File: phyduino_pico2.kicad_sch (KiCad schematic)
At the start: 7 parts, among them J2 PM2.54-1*8, J3 PM2.54-1*10, J4 PM2.54-1*6, J5 PM2.54-1*8, J7 HC-FPC-0.5-22P-CSH20

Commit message: nigthly commit
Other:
- company: (none) -> University of Toronto, Dept. of Physics
- title: (none) -> Phyduino Pico 2
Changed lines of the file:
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@@
 	(generator_version "10.0")
 	(paper "B")
+	(title_block
+		(title "Phyduino Pico 2")
+		(date "2026-05-04")
+		(rev "A")
+		(company "University of Toronto, Dept. of Physics")
+	)
 	(text "GND"
 		(exclude_from_sim no)

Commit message: Made schematic changes : merged usb_pd sheet with wifi sheet. made system regulators adjustable.
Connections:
- net Microcontroller/D18 renamed Microcontroller/D14
- net Microcontroller/D19 renamed Microcontroller/D15
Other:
- sheet Wifi Interface renamed Communication & Power Delivery
- removed sheet USB Power Delivery
- sheet Communication & Power Delivery ports: added I2C1_SCL, I2C1_SDA, PSW_STATUS, USBPD_FLIP, USBPD_GPIO, USBPD_INT, USB_D_N, USB_D_P, WIFI_AT_UART_CTS, WIFI_AT_UART_RTS, WIFI_AT_UART_RX, WIFI_AT_UART_TX, WIFI_DL_UART_RX, WIFI_DL_UART_TX; removed WIFI_UART_CTS, WIFI_UART_RTS, WIFI_UART_RX, WIFI_UART_SEL, WIFI_UART_TX
- sheet Microcontroller ports: added D14, D15, WIFI_DL_UART_RX, WIFI_DL_UART_TX; removed D18, D19, WIFI_UART_SEL
- note added: "D14/SDA"
- note added: "D15/SCL"
- note removed: "D18/SDA"
- note removed: "D19/SCL"
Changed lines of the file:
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@@
 		)
 	)
-	(text "D19/SCL"
+	(text "D15/SCL"
 		(exclude_from_sim no)
 		(at 240.03 101.6 0)
@@
 		)
 	)
-	(text "D18/SDA"
+	(text "D14/SDA"
 		(exclude_from_sim no)
 		(at 240.03 99.06 0)
@@
 	(text "D12/MISO"
 		(exclude_from_sim no)
-		(at 239.522 88.392 0)
+		(at 240.03 88.392 0)
 		(effects
 			(font
@@
 	(text "~D11/MOSI"
 		(exclude_from_sim no)
-		(at 239.268 86.106 0)
+		(at 240.284 86.106 0)
 		(effects
 			(font
@@
 	(wire
 		(pts
-			(xy 71.12 186.69) (xy 107.95 186.69)
-		)
-		(stroke
-			(width 0)
-			(type default)
-		)
-	)
-	(wire
-		(pts
 			(xy 231.14 165.1) (xy 232.41 165.1)
 		)
@@
 	(wire
 		(pts
+			(xy 71.12 165.1) (xy 88.9 165.1)
+		)
+		(stroke
+			(width 0)
+			(type default)
+		)
+	)
+	(wire
+		(pts
 			(xy 232.41 57.15) (xy 143.51 57.15)
 		)
@@
 	(wire
 		(pts
-			(xy 71.12 137.16) (xy 107.95 137.16)
+			(xy 71.12 144.78) (xy 107.95 144.78)
 		)
 		(stroke
@@
 	(wire
 		(pts
+			(xy 71.12 167.64) (xy 88.9 167.64)
+		)
+		(stroke
+			(width 0)
+			(type default)
+		)
+	)
+	(wire
+		(pts
+			(xy 91.44 165.1) (xy 107.95 165.1)
+		)
+		(stroke
+			(width 0)
+			(type default)
+		)
+	)
+	(wire
+		(pts
 			(xy 232.41 54.61) (xy 143.51 54.61)
 		)
@@
 	(wire
 		(pts
+			(xy 88.9 167.64) (xy 91.44 165.1)
+		)
+		(stroke
+			(width 0)
+			(type default)
+		)
+	)
+	(wire
+		(pts
 			(xy 71.12 124.46) (xy 107.95 124.46)
 		)
@@
 	(wire
 		(pts
+			(xy 71.12 147.32) (xy 107.95 147.32)
+		)
+		(stroke
+			(width 0)
+			(type default)
+		)
+	)
+	(wire
+		(pts
 			(xy 48.26 69.85) (xy 48.26 74.93)
 		)
@@
 	(wire
 		(pts
+			(xy 91.44 167.64) (xy 107.95 167.64)
+		)
+		(stroke
+			(width 0)
+			(type default)
+		)
+	)
+	(wire
+		(pts
 			(xy 231.14 127) (xy 232.41 127)
 		)
@@
 	(wire
 		(pts
-			(xy 71.12 139.7) (xy 107.95 139.7)
+			(xy 143.51 114.3) (xy 232.41 114.3)
 		)
 		(stroke
@@
 	(wire
 		(pts
-			(xy 143.51 114.3) (xy 232.41 114.3)
+			(xy 232.41 72.39) (xy 143.51 72.39)
 		)
 		(stroke
@@
 	(wire
 		(pts
-			(xy 232.41 72.39) (xy 143.51 72.39)
+			(xy 58.42 64.77) (xy 45.72 64.77)
 		)
 		(stroke
@@
 	(wire
 		(pts
-			(xy 58.42 64.77) (xy 45.72 64.77)
+			(xy 88.9 165.1) (xy 91.44 167.64)
 		)
 		(stroke
@@
 			)
 		)
-		(pin "D18" bidirectional
+		(pin "D14" bidirectional
 			(at 143.51 97.79 0)
 			(effects
@@
 			)
 		)
-		(pin "D19" bidirectional
+		(pin "D15" bidirectional
 			(at 143.51 100.33 0)
 			(effects
@@
 		)
 		(pin "USB_D_N" bidirectional
-			(at 107.95 139.7 180)
+			(at 107.95 147.32 180)
 			(effects
 				(font
@@
 		)
 		(pin "USB_D_P" bidirectional
-			(at 107.95 137.16 180)
+			(at 107.95 144.78 180)
 			(effects
 				(font
@@
 			)
 		)
-		(pin "WIFI_UART_SEL" output
-			(at 107.95 186.69 180)
+		(pin "WIFI_DL_UART_RX" input
+			(at 107.95 167.64 180)
+			(effects
+				(font
+					(size 1.27 1.27)
+				)
+				(justify left)
+			)
+		)
+		(pin "WIFI_DL_UART_TX" output
+			(at 107.95 165.1 180)
 			(effects
 				(font
@@
 	(sheet
 		(at 39.37 111.76)
-		(size 31.75 30.48)
+		(size 31.75 80.01)
 		(exclude_from_sim no)
 		(in_bom yes)
@@
 			(color 255 255 194 1)
 		)
-		(property "Sheetname" "USB Power Delivery"
+		(property "Sheetname" "Communication & Power Delivery"
 			(at 39.37 111.0484 0)
 			(show_name no)
@@
 			)
 		)
-		(property "Sheetfile" "phyduino_pico2_usbpd.kicad_sch"
-			(at 39.37 142.8246 0)
+		(property "Sheetfile" "phyduino_pico2_wifi.kicad_sch"
+			(at 39.37 192.3546 0)
 			(hide yes)
 			(show_name no)
@@
 			)
 		)
-		(pin "I2C1_SCL" input
-			(at 71.12 116.84 0)
+		(pin "WIFI_ENA" input
+			(at 71.12 189.23 0)
 			(effects
 				(font
@@
 			)
 		)
-		(pin "I2C1_SDA" bidirectional
-			(at 71.12 114.3 0)
+		(pin "WIFI_AT_UART_CTS" output
+			(at 71.12 179.07 0)
 			(effects
 				(font
@@
 			)
 		)
-		(pin "USBPD_FLIP" output
-			(at 71.12 124.46 0)
+		(pin "WIFI_AT_UART_RTS" input
+			(at 71.12 181.61 0)
 			(effects
 				(font
@@
 			)
 		)
-		(pin "USBPD_GPIO" output
-			(at 71.12 127 0)
+		(pin "WIFI_AT_UART_RX" input
+			(at 71.12 176.53 0)
 			(effects
 				(font
@@
 			)
 		)
-		(pin "USBPD_INT" output
-			(at 71.12 121.92 0)
+		(pin "WIFI_AT_UART_TX" output
+			(at 71.12 173.99 0)
 			(effects
 				(font
@@
 			)
 		)
-		(pin "PSW_STATUS" output
-			(at 71.12 130.81 0)
+		(pin "WIFI_DL_UART_RX" input
+			(at 71.12 167.64 0)
 			(effects
 				(font
@@
 			)
 		)
-		(pin "USB_D_N" bidirectional
-			(at 71.12 139.7 0)
+		(pin "WIFI_DL_UART_TX" output
+			(at 71.12 165.1 0)
 			(effects
 				(font
@@
 			)
 		)
-		(pin "USB_D_P" bidirectional
-			(at 71.12 137.16 0)
+		(pin "I2C1_SCL" input
+			(at 71.12 116.84 0)
 			(effects
 				(font
@@
 			)
 		)
-		(instances
-			(project "phyduino_pico2"
-				(path "/42309c5d-9d7a-429d-b353-e8927a604374"
-					(page "4")
-				)
-			)
-		)
-	)
-	(sheet
-		(at 39.37 171.45)
-		(size 31.75 20.32)
-		(exclude_from_sim no)
-		(in_bom yes)
-		(on_board yes)
-		(dnp no)
-		(fields_autoplaced yes)
-		(stroke
-			(width 0.1524)
-			(type solid)
-		)
-		(fill
-			(color 255 255 194 1)
-		)
-		(property "Sheetname" "Wifi Interface"
-			(at 39.37 170.7384 0)
-			(show_name no)
-			(do_not_autoplace no)
-			(effects
-				(font
-					(size 1.27 1.27)
-				)
-				(justify left bottom)
-			)
-		)
-		(property "Sheetfile" "phyduino_pico2_wifi.kicad_sch"
-			(at 39.37 192.3546 0)
-			(hide yes)
-			(show_name no)
-			(do_not_autoplace no)
+		(pin "I2C1_SDA" bidirectional
+			(at 71.12 114.3 0)
 			(effects
 				(font
 					(size 1.27 1.27)
 				)
-				(justify left top)
+				(justify right)
 			)
 		)
-		(pin "WIFI_ENA" input
-			(at 71.12 189.23 0)
+		(pin "PSW_STATUS" output
+			(at 71.12 130.81 0)
 			(effects
 				(font
@@
 			)
 		)
-		(pin "WIFI_UART_CTS" output
-			(at 71.12 179.07 0)
+		(pin "USBPD_FLIP" output
+			(at 71.12 124.46 0)
 			(effects
 				(font
@@
 			)
 		)
-		(pin "WIFI_UART_RTS" input
-			(at 71.12 181.61 0)
+		(pin "USBPD_GPIO" output
+			(at 71.12 127 0)
 			(effects
 				(font
@@
 			)
 		)
-		(pin "WIFI_UART_RX" input
-			(at 71.12 176.53 0)
+		(pin "USBPD_INT" output
+			(at 71.12 121.92 0)
 			(effects
 				(font
@@
 			)
 		)
-		(pin "WIFI_UART_TX" output
-			(at 71.12 173.99 0)
+		(pin "USB_D_N" bidirectional
+			(at 71.12 147.32 0)
 			(effects
 				(font
@@
 			)
 		)
-		(pin "WIFI_UART_SEL" input
-			(at 71.12 186.69 0)
+		(pin "USB_D_P" bidirectional
+			(at 71.12 144.78 0)
 			(effects
 				(font

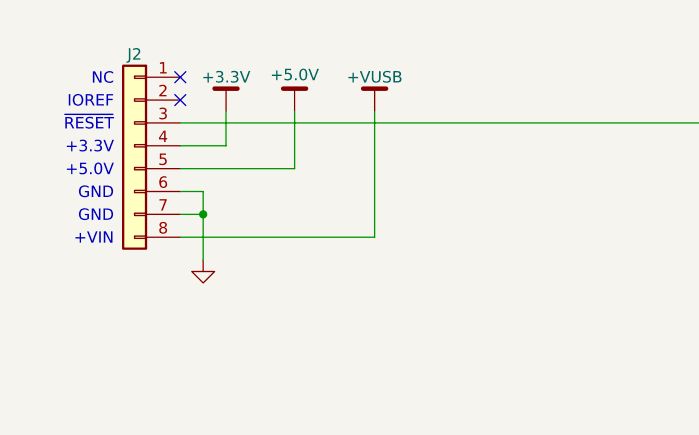
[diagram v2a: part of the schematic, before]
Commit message: Made changes to the power tree to allow +Vin to power the board.
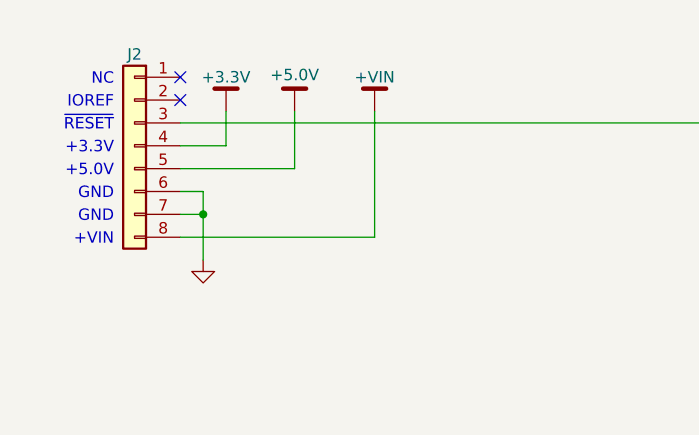
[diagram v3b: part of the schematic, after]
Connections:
- net +VUSB renamed +VIN
